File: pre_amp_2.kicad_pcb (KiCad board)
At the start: 2 copper layers, 61.3 x 49.9 mm, 48 parts, among them J1 IN, J11 SW2_3, J12 SW2_1, J13 SW2_4, J14 SW5_3, J15 VR5_1, J16 OUT, J2 Vin, J3 GND, J4 VR1_1, J5 VR2_1, J6 VR1_3, J7 VR1_2, J8 SW1, J9 SW2, U1 TL072, U2 ICL7660

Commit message: 配置修正
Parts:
- moved C6 1.27 mm to (127.5, 107.2)
- moved J5 1.27 mm to (122.4, 111.8)
- moved C5 1.18 mm to (122.8, 100.8)
- moved D1 1.02 mm to (173.0, 106.2)
- moved D2 1.02 mm to (165.4, 109.0)
- moved J13 1.02 mm to (173.0, 117.9)
- moved R10 1.02 mm to (165.4, 96.0)
- moved D3 1.02 mm to (173.0, 111.8)
- moved D4 1.02 mm to (165.4, 114.6)
- moved J12 1.02 mm to (173.0, 102.9)
- moved J4 0.92 mm to (119.1, 106.6)
- moved J9 0.90 mm to (163.7, 118.0)
- moved H3 0.46 mm to (118.6, 118.2)
- moved C10 0.38 mm to (134.9, 118.5)
- moved J7 0.38 mm to (131.8, 118.5)
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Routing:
- net Net-(J16-Pin_1): track 6.96 -> 7.80 mm
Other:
- board size 61.3 x 49.9 mm -> 61.2 x 49.3 mm

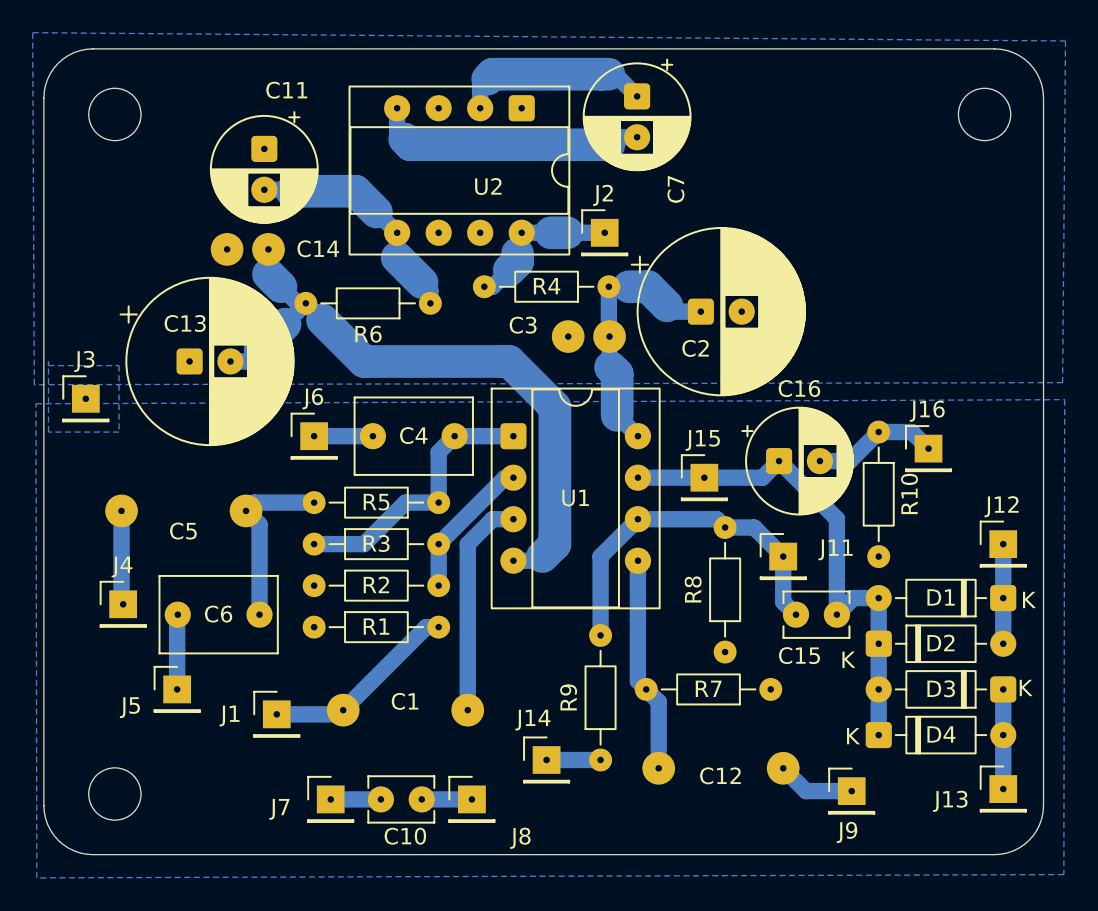
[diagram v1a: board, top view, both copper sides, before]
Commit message: LED用の抵抗を追加
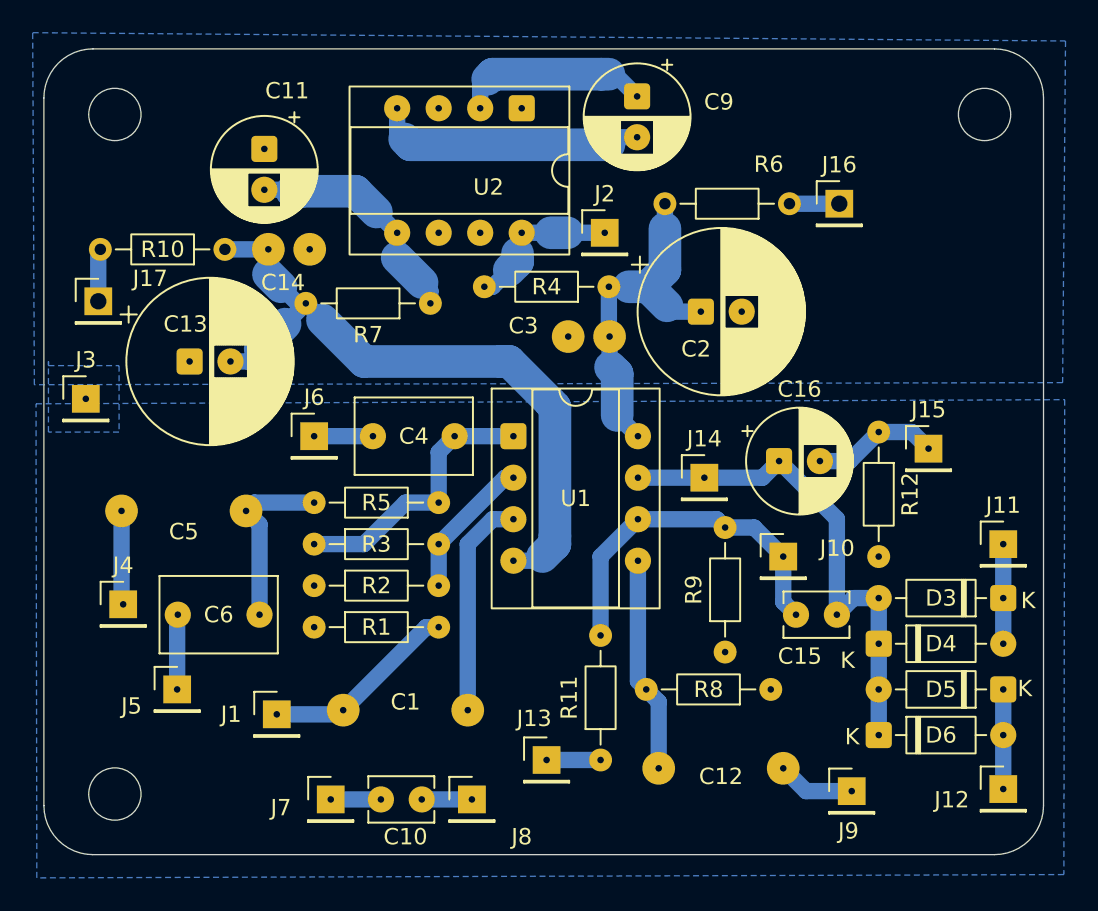
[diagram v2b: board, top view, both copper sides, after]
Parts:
- added J16: +Led, Connector_PinHeader_2.54mm:PinHeader_1x01_P2.54mm_Vertical, F.Cu at (162.9, 82.0)
- added J17: -Led, Connector_PinHeader_2.54mm:PinHeader_1x01_P2.54mm_Vertical, F.Cu at (117.6, 88.0)
- added R10: 2.2k, Resistor_THT:R_Axial_DIN0204_L3.6mm_D1.6mm_P7.62mm_Horizontal, F.Cu at (125.3, 84.8)
- added R6: 2.2k, Resistor_THT:R_Axial_DIN0204_L3.6mm_D1.6mm_P7.62mm_Horizontal, F.Cu at (159.9, 82.0)
- moved C14 2.55 mm to (129.3, 84.8), turned to 0 degrees
- renumbered C7 to C9, D1 to D3, D2 to D4, D3 to D5, D4 to D6, J11 to J10, J12 to J11, J13 to J12, J14 to J13, J15 to J14, J16 to J15, R9 to R11, R10 to R12, R6 to R7, R7 to R8, R8 to R9
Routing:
- net Net-(U1C-V+): track 16.1 -> 21.7 mm
- net Net-(D2-K): track 0.00 -> 3.23 mm
- net Net-(D1-A): track 0.00 -> 3.05 mm
- net Net-(U1C-V-): track 42.0 -> 44.7 mm
